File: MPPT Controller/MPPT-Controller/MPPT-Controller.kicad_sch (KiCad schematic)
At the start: 1 part, among them U1 ADS1115IDGS

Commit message: Update
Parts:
- added C1, C2, C3, C4, C5, C6: 0.1u, Capacitor_SMD:C_0603_1608Metric_Pad1.08x0.95mm_HandSolder, symbol Device:C
- added J1, J2, J3: Conn_01x02_Pin, symbol Connector:Conn_01x02_Pin
- added K1: JQC-3FF-005-1Z, Relay_THT:Relay_SPDT_Hongfa_JQC-3FF_0XX-1Z, symbol Relay:JQC-3FF-005-1Z
- added LR1, LR2, LR3, LR4: 0.1R, symbol Device:R
- added Q1: BC817, Package_TO_SOT_SMD:SOT-23_Handsoldering, symbol Transistor_BJT:BC817
- added R1: 330R, Resistor_SMD:R_0603_1608Metric_Pad0.98x0.95mm_HandSolder, symbol Device:R
- added R2, R3, R4, R5, R7, R8: 50R, symbol Device:R
- added R6: R, symbol Device:R
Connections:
- net IdiffA: now reaches U1.4 (AIN0)
- net IdiffA: now also R2.2, R4.2
- net IdiffB: now reaches U1.5 (AIN1)
- net IdiffB: now also R3.2, R5.2
- new net: Q1.1 (B), R1.2
- new net: LR3.2, LR4.1
- new net: LR1.2, LR2.1
- new net: J3.2 (Pin_2), R5.1
- new net: J3.1 (Pin_1), R4.1
- new net +3V3: Q1.3 (C)
- new net GND: C1.2, C2.2, C3.2, C4.2, C5.2, C6.2, J1.2 (Pin_2), J2.2 (Pin_2)
- new net OdiffA: R7.2
- new net OdiffB: R8.2
- new net Range: R1.1
- new net Vaux: C3.1, C4.1
- new net Vin: C1.1, J1.1 (Pin_1), LR1.1, R2.1
- new net Vinter: C2.1, C5.1, LR2.2, LR3.1, R3.1, R7.1
- new net Vout: C6.1, J2.1 (Pin_1), LR4.2, R8.1
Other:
- note added: "Input and Output Connectors"
- moved on the sheet: U1

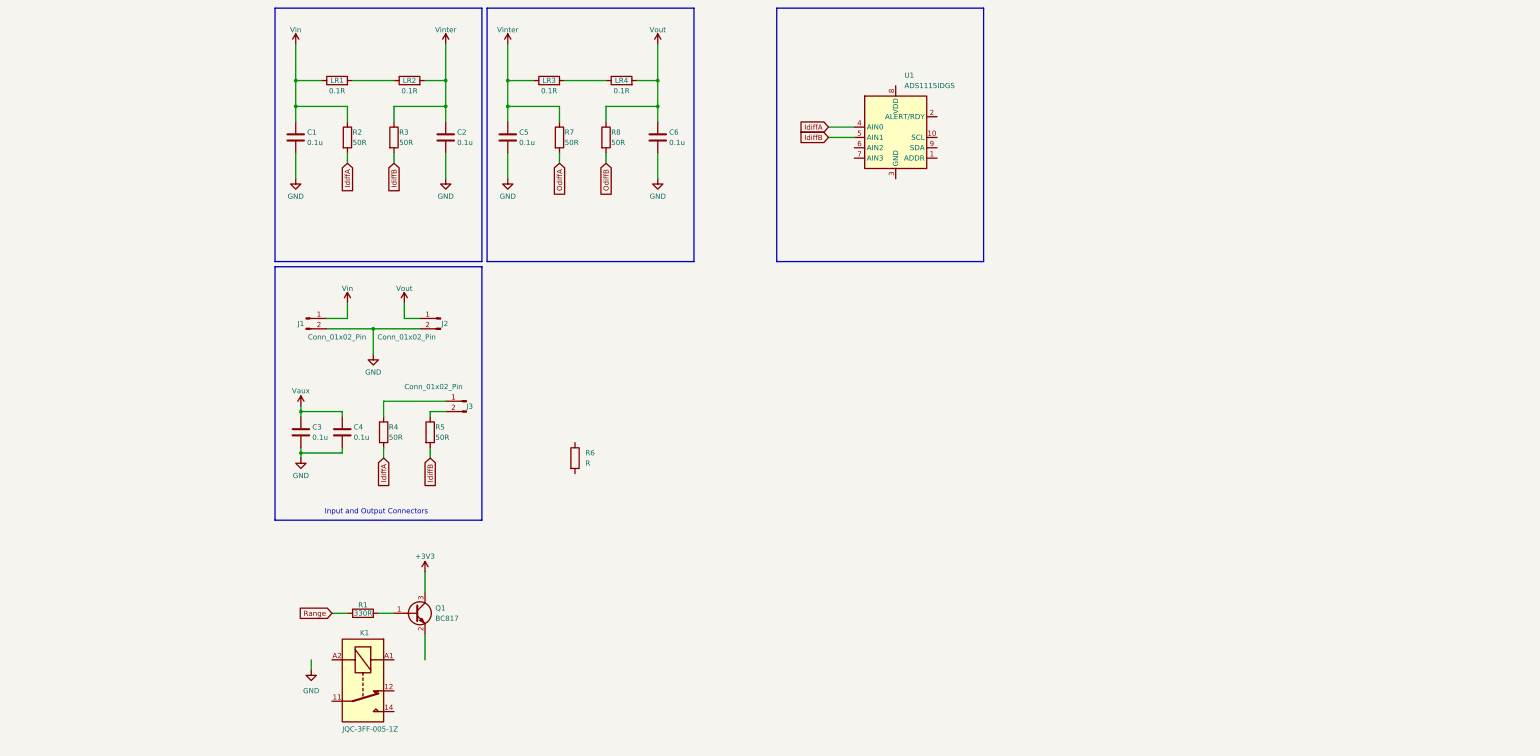
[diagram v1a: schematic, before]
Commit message: Add USB Power
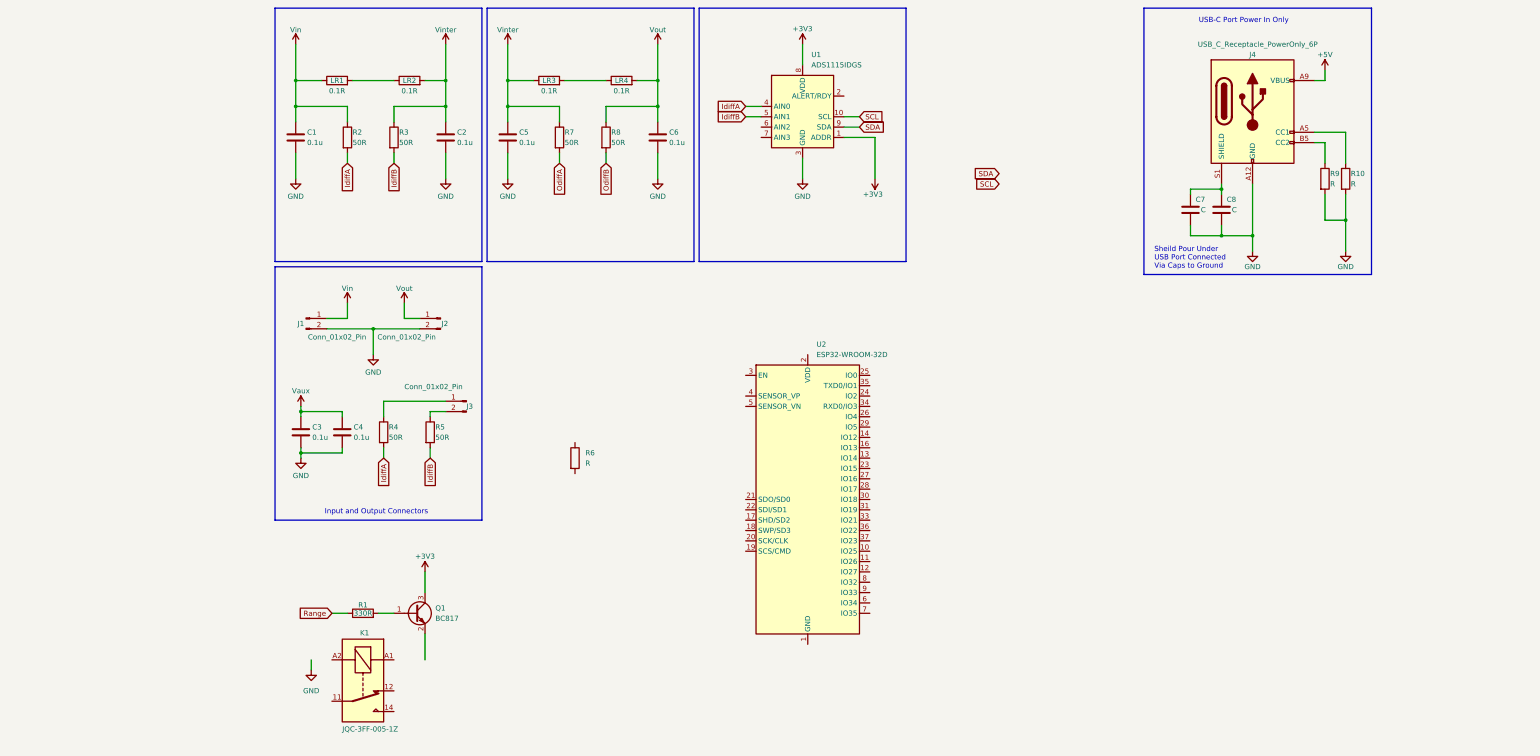
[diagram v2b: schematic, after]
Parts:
- added C7, C8: C, Capacitor_SMD:C_0603_1608Metric_Pad1.08x0.95mm_HandSolder, symbol Device:C
- added J4: USB_C_Receptacle_PowerOnly_6P, CustomLibrary:USB-C Receptacle Power Only THT, symbol Connector:USB_C_Receptacle_PowerOnly_6P
- added R10, R9: R, Capacitor_SMD:C_0603_1608Metric_Pad1.08x0.95mm_HandSolder, symbol Device:R
- added U2: ESP32-WROOM-32D, RF_Module:ESP32-WROOM-32D, symbol RF_Module:ESP32-WROOM-32D
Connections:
- net +3V3: now also U1.1 (ADDR), U1.8 (VDD)
- net GND: now also U1.3 (GND), C7.2, C8.2, J4.A12 (GND), J4.B12 (GND), R10.2, R9.2
- net SCL: now reaches U1.10 (SCL)
- net SDA: now reaches U1.9 (SDA)
- new net: J4.A5 (CC1), R10.1
- new net: J4.B5 (CC2), R9.1
- new net: C7.1, C8.1, J4.S1 (SHIELD)
- new net: U2.1 (GND), U2.15 (GND), U2.38 (GND), U2.39 (GND)
- new net +5V: J4.A9 (VBUS), J4.B9 (VBUS)
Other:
- note added: "Sheild Pour Under USB Port Connected Via Caps to Ground"
- note added: "USB-C Port Power In Only"
- moved on the sheet: U1

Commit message: Connect SDA SCL
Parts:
- added BOOT1, RESET1: SW_Push, CustomLibrary:SwitchCustom, symbol Switch:SW_Push
- added FLASH1: Conn_01x06_Pin, Connector_PinHeader_2.54mm:PinHeader_2x03_P2.54mm_Vertical, symbol Connector:Conn_01x06_Pin
- added R11, R12: 10k, Resistor_SMD:R_0805_2012Metric_Pad1.20x1.40mm_HandSolder, symbol Device:R
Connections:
- net +3V3: now also FLASH1.2 (Pin_2), R11.2, R12.2
- net GND: now also BOOT1.1, FLASH1.1 (Pin_1), RESET1.1
- net SCL: now also U2.36 (IO22)
- net SDA: now also U2.33 (IO21)
- net Sx: now reaches U2.24 (IO2)
- net BOOT: now reaches U2.25 (IO0)
- net BOOT: now also BOOT1.2, FLASH1.3 (Pin_3), R12.1
- net RST: now reaches U2.3 (EN)
- net RST: now also FLASH1.4 (Pin_4), R11.1, RESET1.2
- net Rx: now reaches U2.34 (RXD0/IO3)
- net Rx: now also FLASH1.6 (Pin_6)
- net Tx: now reaches U2.35 (TXD0/IO1)
- net Tx: now also FLASH1.5 (Pin_5)
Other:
- note added: "Boot Button"
- note added: "Reset Button"
- note added: "UART - For Flash"

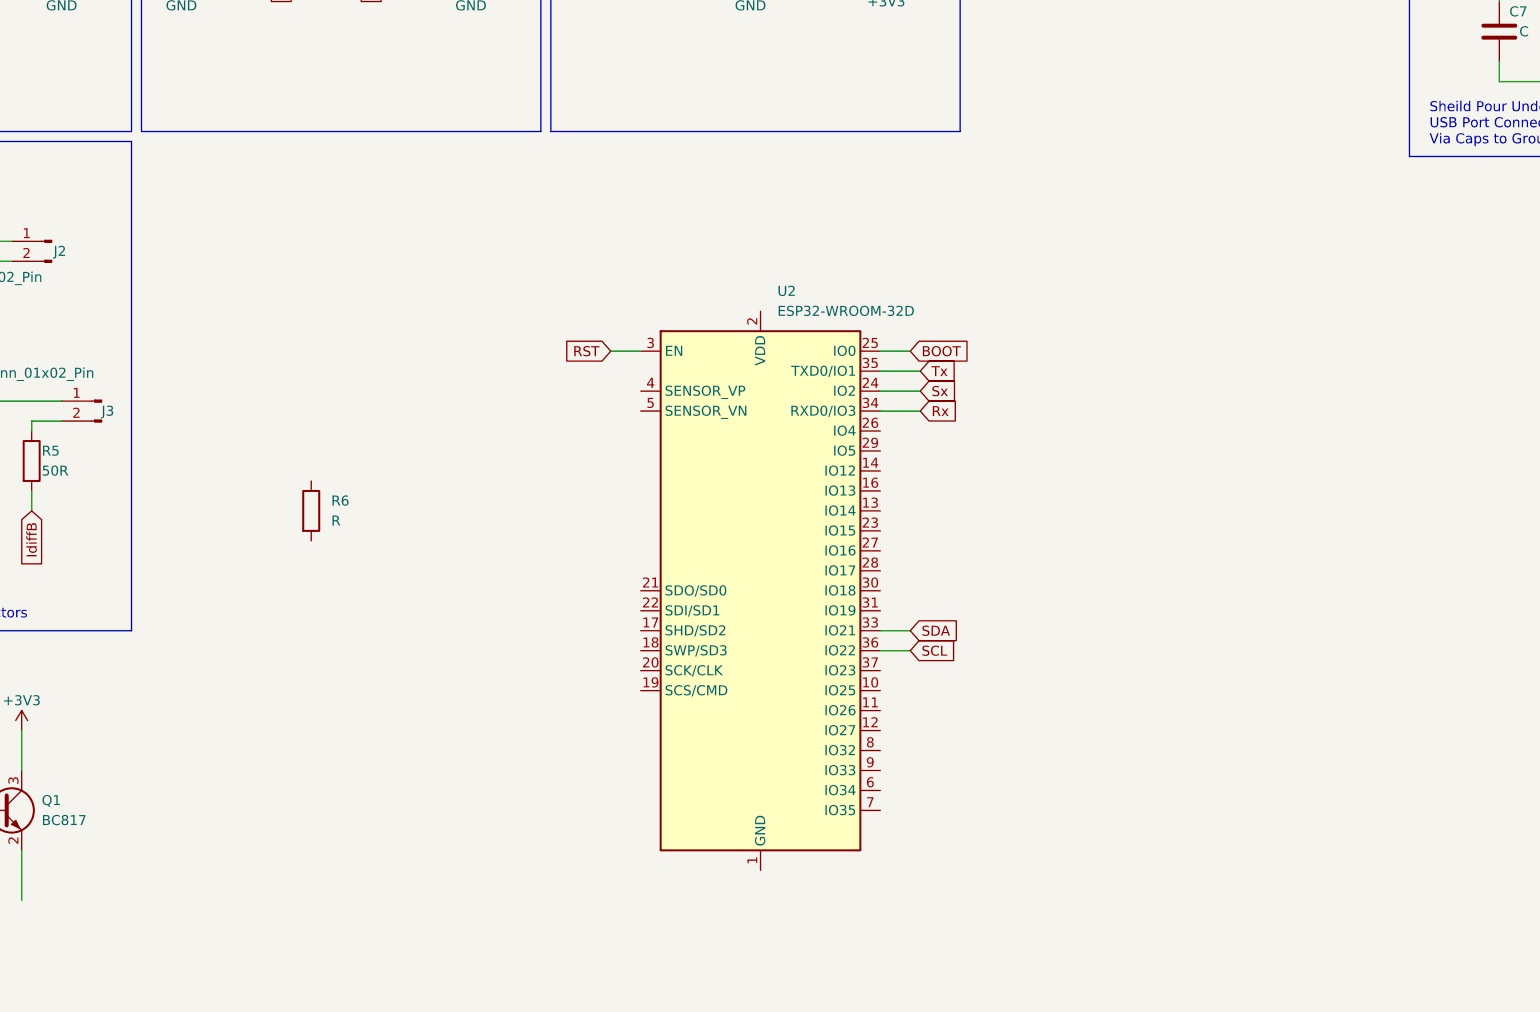
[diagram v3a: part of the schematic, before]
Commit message: Add Connectors
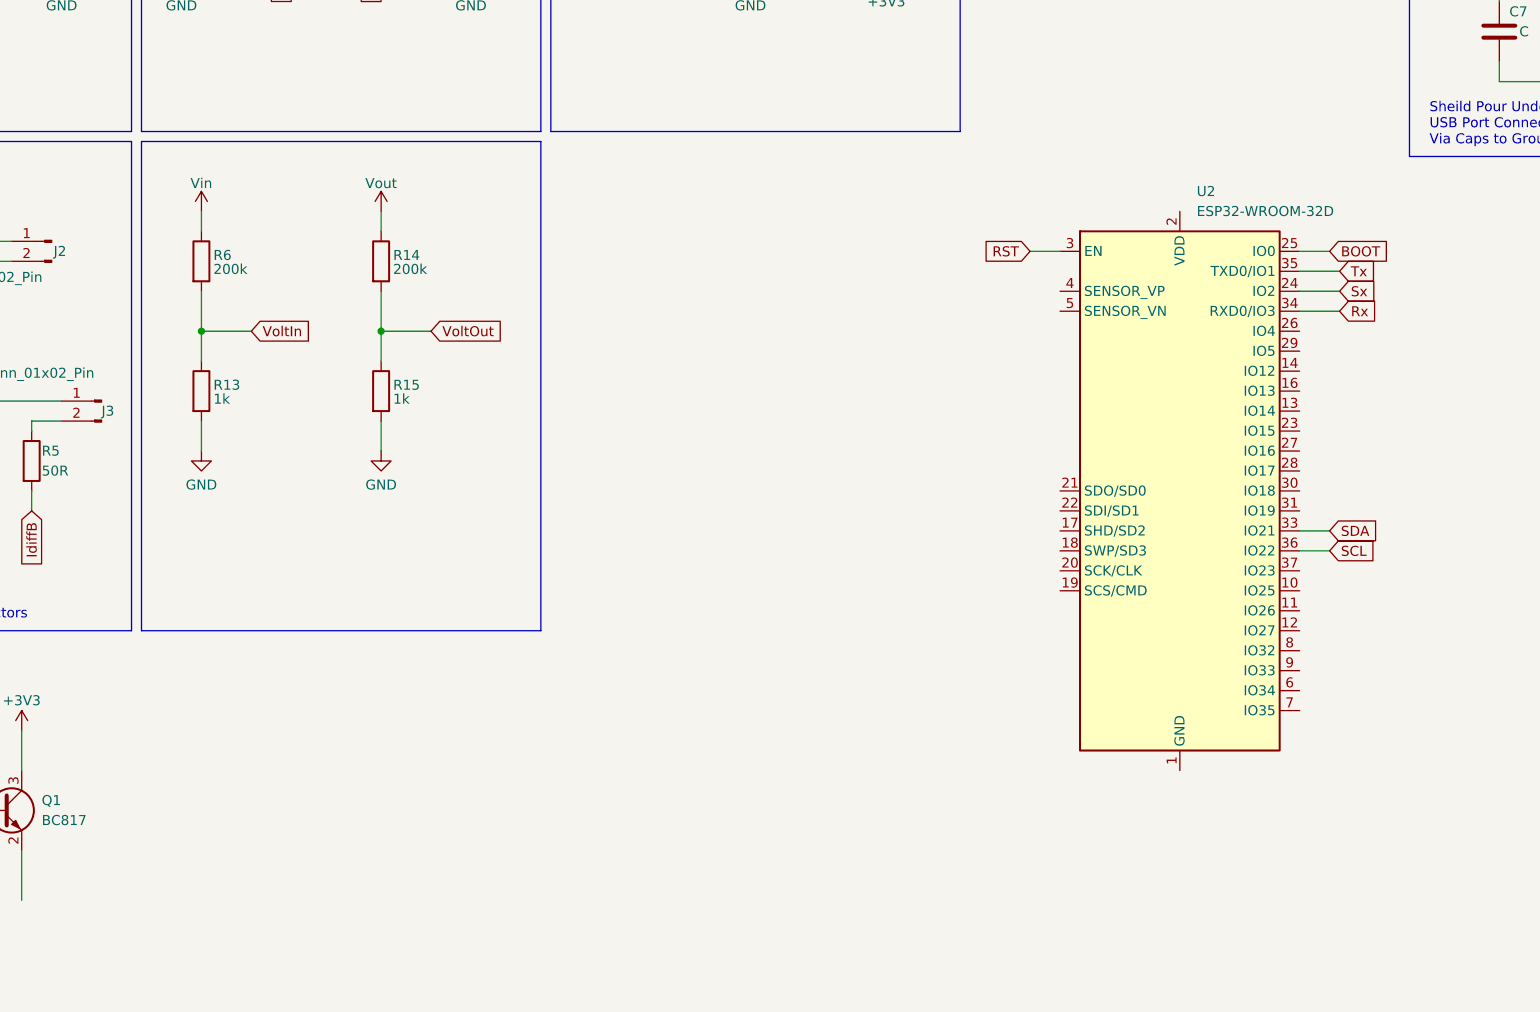
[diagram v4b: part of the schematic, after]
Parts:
- added R13, R15: 1k, symbol Device:R
- added R14: 200k, symbol Device:R
- R6: value R -> 200k
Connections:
- net GND: now also R13.2, R15.2
- net Vin: now also R6.1
- net Vout: now also R14.1
- net VoltIn: now reaches R6.2
- net VoltIn: now also R13.1
- new net VoltOut: R14.2, R15.1
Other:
- moved on the sheet: R6, U2
